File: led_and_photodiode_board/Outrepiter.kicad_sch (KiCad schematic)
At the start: 10 parts, among them U10 LM2901

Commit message: ledphoto исправлена микросхема
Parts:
- removed U10: LM2901, symbol Comparator:LM2901
- added U1: LM2901, symbol Comparator:LM2901
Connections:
- net +24V: now also U1.3 (V+)
- net GNDA: now also U1.12 (V-)
- net OUT1: now also U1.2
- net OUT2: now also U1.1
- net OUT3: now also U1.13
- net OUT4: now also U1.14
- net at R19.2: now also U1.10 (-)
- net at R23.2: now also U1.11 (+)
- net at R21.2: now also U1.5 (+)
- net at R26.2: now also U1.4 (-)
- net at R24.2: now also U1.9 (+)
- net at R20.2: now also U1.8 (-)
- net at R22.2: now also U1.7 (+)
- net at R18.2: now also U1.6 (-)

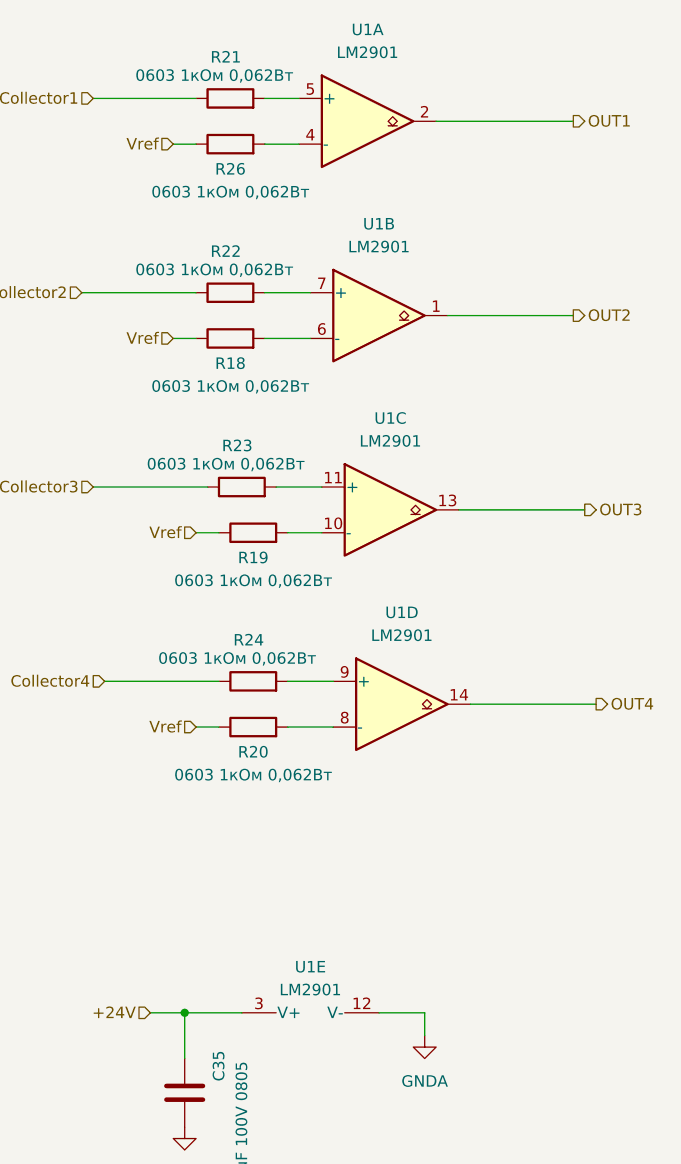
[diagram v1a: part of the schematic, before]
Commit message: ledphoto коррекция схемы
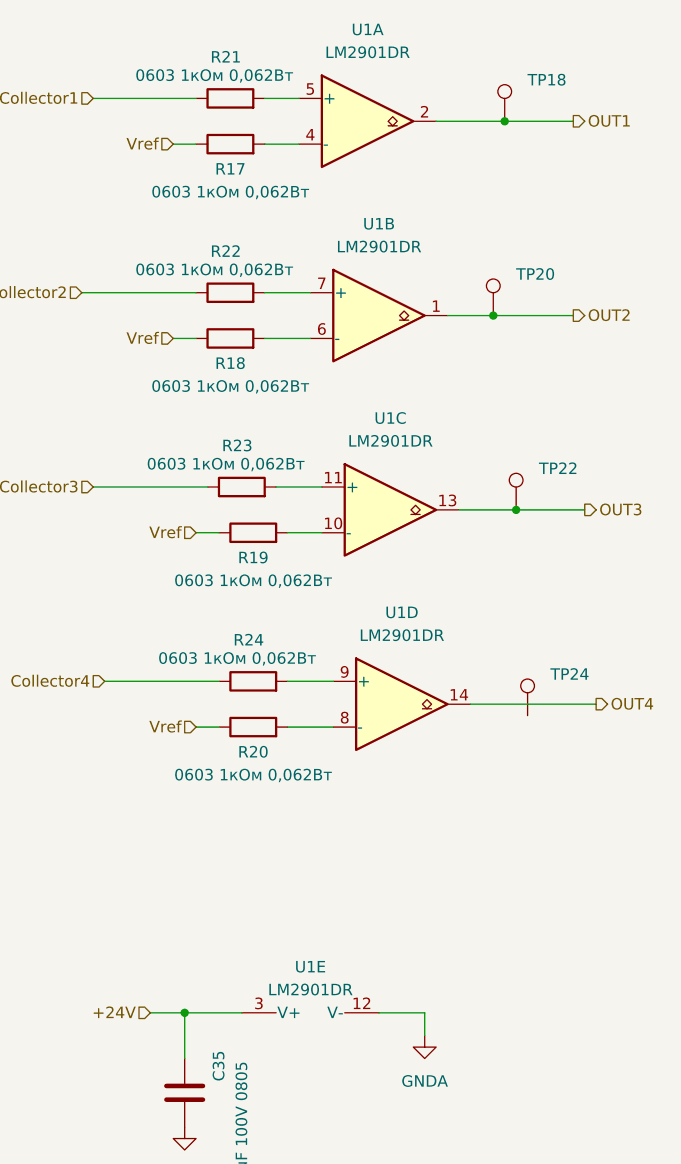
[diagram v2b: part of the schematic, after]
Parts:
- added TP18, TP20, TP22, TP24: TestPoint, TestPoint:TestPoint_Pad_D1.0mm, symbol Connector:TestPoint
- C35: footprint PCM_Resistor_SMD_AKL:R_0805_2012Metric_Pad1.20x1.40mm_HandSolder -> Capacitor_SMD:C_0805_2012Metric
- R17: renamed from R26; footprint (none) -> Resistor_SMD:R_0603_1608Metric
- R18, R19, R20, R21, R22, R23, R24: footprint (none) -> Resistor_SMD:R_0603_1608Metric
- U1: value LM2901 -> LM2901DR; footprint (none) -> Package_SO:SOIC-14_3.9x8.7mm_P1.27mm
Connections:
- net OUT1: now also TP18.1
- net OUT2: now also TP20.1
- net OUT3: now also TP22.1

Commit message: ledphoto обновлена схема и pcb
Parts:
- C35: value 0,1uF 100V 0805 -> 0805 0,1uF 100V
- R17, R18, R19, R20, R21, R22, R23, R24: value 0603 1кОм 0,062Вт -> 0603 1 кОм±5%-0,062Вт
- U1: value LM2901DR -> LM2901DR (SOIC-14)
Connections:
- net OUT4: now also TP24.1
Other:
- moved on the sheet: TP24
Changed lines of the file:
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@@
 		(color 0 0 0 0)
 	)
+	(junction
+		(at 160.02 118.11)
+		(diameter 0)
+		(color 0 0 0 0)
+	)
 	(wire
 		(pts
@@
 	(wire
 		(pts
+			(xy 160.02 118.11) (xy 153.67 118.11)
+		)
+		(stroke
+			(width 0)
+			(type default)
+		)
+	)
+	(wire
+		(pts
 			(xy 152.4 96.52) (xy 158.75 96.52)
 		)
@@
 	(wire
 		(pts
+			(xy 161.29 53.34) (xy 157.48 53.34)
+		)
+		(stroke
+			(width 0)
+			(type default)
+		)
+	)
+	(wire
+		(pts
+			(xy 162.56 74.93) (xy 156.21 74.93)
+		)
+		(stroke
+			(width 0)
+			(type default)
+		)
+	)
+	(wire
+		(pts
 			(xy 121.92 152.4) (xy 121.92 157.48)
 		)
@@
 	(wire
 		(pts
-			(xy 156.21 74.93) (xy 165.1 74.93)
+			(xy 161.29 96.52) (xy 158.75 96.52)
+		)
+		(stroke
+			(width 0)
+			(type default)
+		)
+	)
+	(wire
+		(pts
+			(xy 162.56 73.66) (xy 165.1 73.66)
 		)
 		(stroke
@@
 	(wire
 		(pts
-			(xy 153.67 118.11) (xy 167.64 118.11)
-		)
-		(stroke
-			(width 0)
-			(type default)
-		)
-	)
-	(wire
-		(pts
 			(xy 121.92 152.4) (xy 128.27 152.4)
 		)
@@
 	(wire
 		(pts
+			(xy 161.29 95.25) (xy 161.29 96.52)
+		)
+		(stroke
+			(width 0)
+			(type default)
+		)
+	)
+	(wire
+		(pts
 			(xy 120.65 55.88) (xy 123.19 55.88)
 		)
@@
 	(wire
 		(pts
-			(xy 157.48 53.34) (xy 165.1 53.34)
+			(xy 161.29 52.07) (xy 165.1 52.07)
 		)
 		(stroke
@@
 	(wire
 		(pts
+			(xy 160.02 118.11) (xy 167.64 118.11)
+		)
+		(stroke
+			(width 0)
+			(type default)
+		)
+	)
+	(wire
+		(pts
 			(xy 130.81 55.88) (xy 134.62 55.88)
 		)
@@
 	(wire
 		(pts
-			(xy 158.75 96.52) (xy 166.37 96.52)
+			(xy 161.29 95.25) (xy 166.37 95.25)
+		)
+		(stroke
+			(width 0)
+			(type default)
+		)
+	)
+	(wire
+		(pts
+			(xy 162.56 73.66) (xy 162.56 74.93)
+		)
+		(stroke
+			(width 0)
+			(type default)
+		)
+	)
+	(wire
+		(pts
+			(xy 161.29 52.07) (xy 161.29 53.34)
 		)
 		(stroke
@@
 	(hierarchical_label "OUT2"
 		(shape output)
-		(at 165.1 74.93 0)
+		(at 165.1 73.66 0)
 		(fields_autoplaced yes)
 		(effects
@@
 	(hierarchical_label "OUT1"
 		(shape output)
-		(at 165.1 53.34 0)
+		(at 165.1 52.07 0)
 		(fields_autoplaced yes)
 		(effects
@@
 	(hierarchical_label "OUT3"
 		(shape output)
-		(at 166.37 96.52 0)
+		(at 166.37 95.25 0)
 		(fields_autoplaced yes)
 		(effects
@@
 			)
 		)
-		(property "Value" "LM2901DR"
+		(property "Value" "LM2901DR (SOIC-14)"
 			(at 144.78 88.9 0)
 			(effects
@@
 			)
 		)
-		(property "Value" "0603 1кОм 0,062Вт"
+		(property "Value" "0603 1 кОм±5%-0,062Вт"
 			(at 125.222 48.26 90)
 			(effects
@@
 			)
 		)
-		(property "Value" "0603 1кОм 0,062Вт"
+		(property "Value" "0603 1 кОм±5%-0,062Вт"
 			(at 127.762 113.03 90)
 			(effects
@@
 			)
 		)
-		(property "Value" "LM2901DR"
+		(property "Value" "LM2901DR (SOIC-14)"
 			(at 146.05 110.49 0)
 			(effects
@@
 			)
 		)
-		(property "Value" "0603 1кОм 0,062Вт"
+		(property "Value" "0603 1 кОм±5%-0,062Вт"
 			(at 127 61.214 90)
 			(effects
@@
 			)
 		)
-		(property "Value" "LM2901DR"
+		(property "Value" "LM2901DR (SOIC-14)"
 			(at 142.24 45.72 0)
 			(effects
@@
 			)
 		)
-		(property "Value" "0603 1кОм 0,062Вт"
+		(property "Value" "0603 1 кОм±5%-0,062Вт"
 			(at 129.54 125.984 90)
 			(effects
@@
 			)
 		)
-		(property "Value" "0603 1кОм 0,062Вт"
+		(property "Value" "0603 1 кОм±5%-0,062Вт"
 			(at 129.54 104.394 90)
 			(effects
@@
 			)
 		)
-		(property "Value" "0,1uF 100V 0805"
+		(property "Value" "0805 0,1uF 100V"
 			(at 128.27 172.72 90)
 			(effects
@@
 			)
 		)
-		(property "Value" "0603 1кОм 0,062Вт"
+		(property "Value" "0603 1 кОм±5%-0,062Вт"
 			(at 125.222 69.85 90)
 			(effects
@@
 			)
 		)
-		(property "Value" "0603 1кОм 0,062Вт"
+		(property "Value" "0603 1 кОм±5%-0,062Вт"
 			(at 126.492 91.44 90)
 			(effects
@@
 			)
 		)
-		(property "Value" "0603 1кОм 0,062Вт"
+		(property "Value" "0603 1 кОм±5%-0,062Вт"
 			(at 127 82.804 90)
 			(effects
@@
 			)
 		)
-		(property "Value" "LM2901DR"
+		(property "Value" "LM2901DR (SOIC-14)"
 			(at 143.51 67.31 0)
 			(effects
@@
 	(symbol
 		(lib_id "Connector:TestPoint")
-		(at 160.02 119.38 0)
+		(at 160.02 118.11 0)
 		(unit 1)
 		(exclude_from_sim no)
@@
 		(fields_autoplaced yes)
 		(property "Reference" "TP24"
-			(at 162.56 114.8079 0)
+			(at 162.56 113.5379 0)
 			(effects
 				(font
@@
 		)
 		(property "Value" "TestPoint"
-			(at 162.56 117.3479 0)
+			(at 162.56 116.0779 0)
 			(effects
 				(font
@@
 		)
 		(property "Footprint" "TestPoint:TestPoint_Pad_D1.0mm"
-			(at 165.1 119.38 0)
+			(at 165.1 118.11 0)
 			(effects
 				(font
@@
 		)
 		(property "Datasheet" "~"
-			(at 165.1 119.38 0)
+			(at 165.1 118.11 0)
 			(effects
 				(font
@@
 		)
 		(property "Description" "test point"
-			(at 160.02 119.38 0)
+			(at 160.02 118.11 0)
 			(effects
 				(font
@@
 			)
 		)
-		(property "Value" "LM2901DR"
+		(property "Value" "LM2901DR (SOIC-14)"
 			(at 135.89 149.86 90)
 			(effects

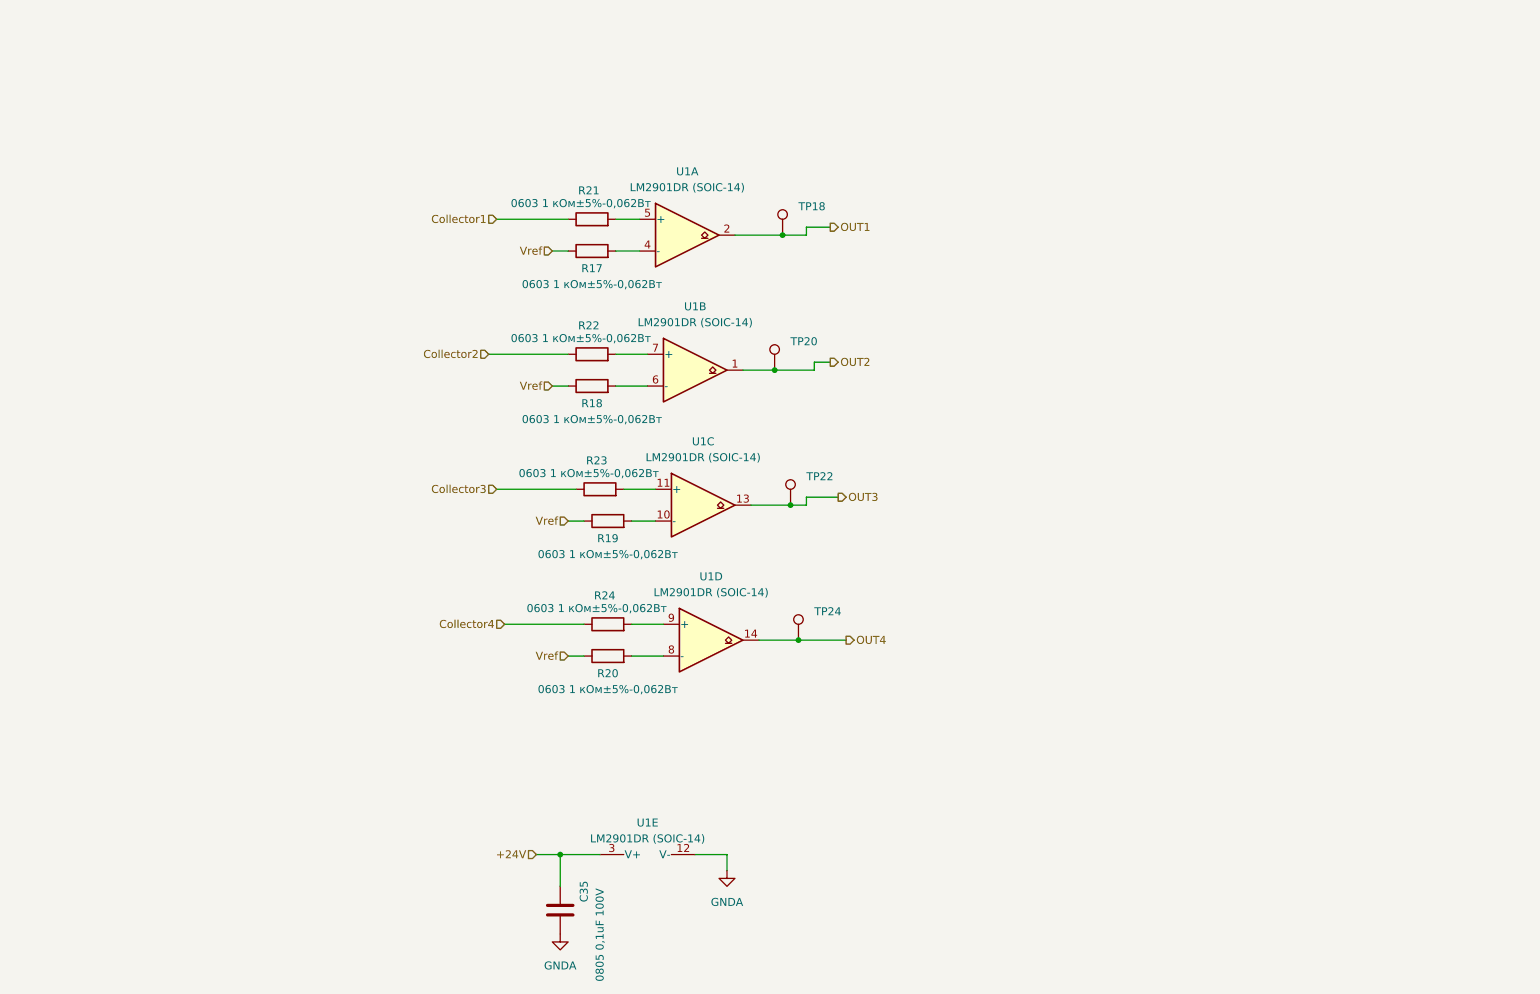
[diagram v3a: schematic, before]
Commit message: ledphoto замена компаратора на операционник, добавлен снаббер
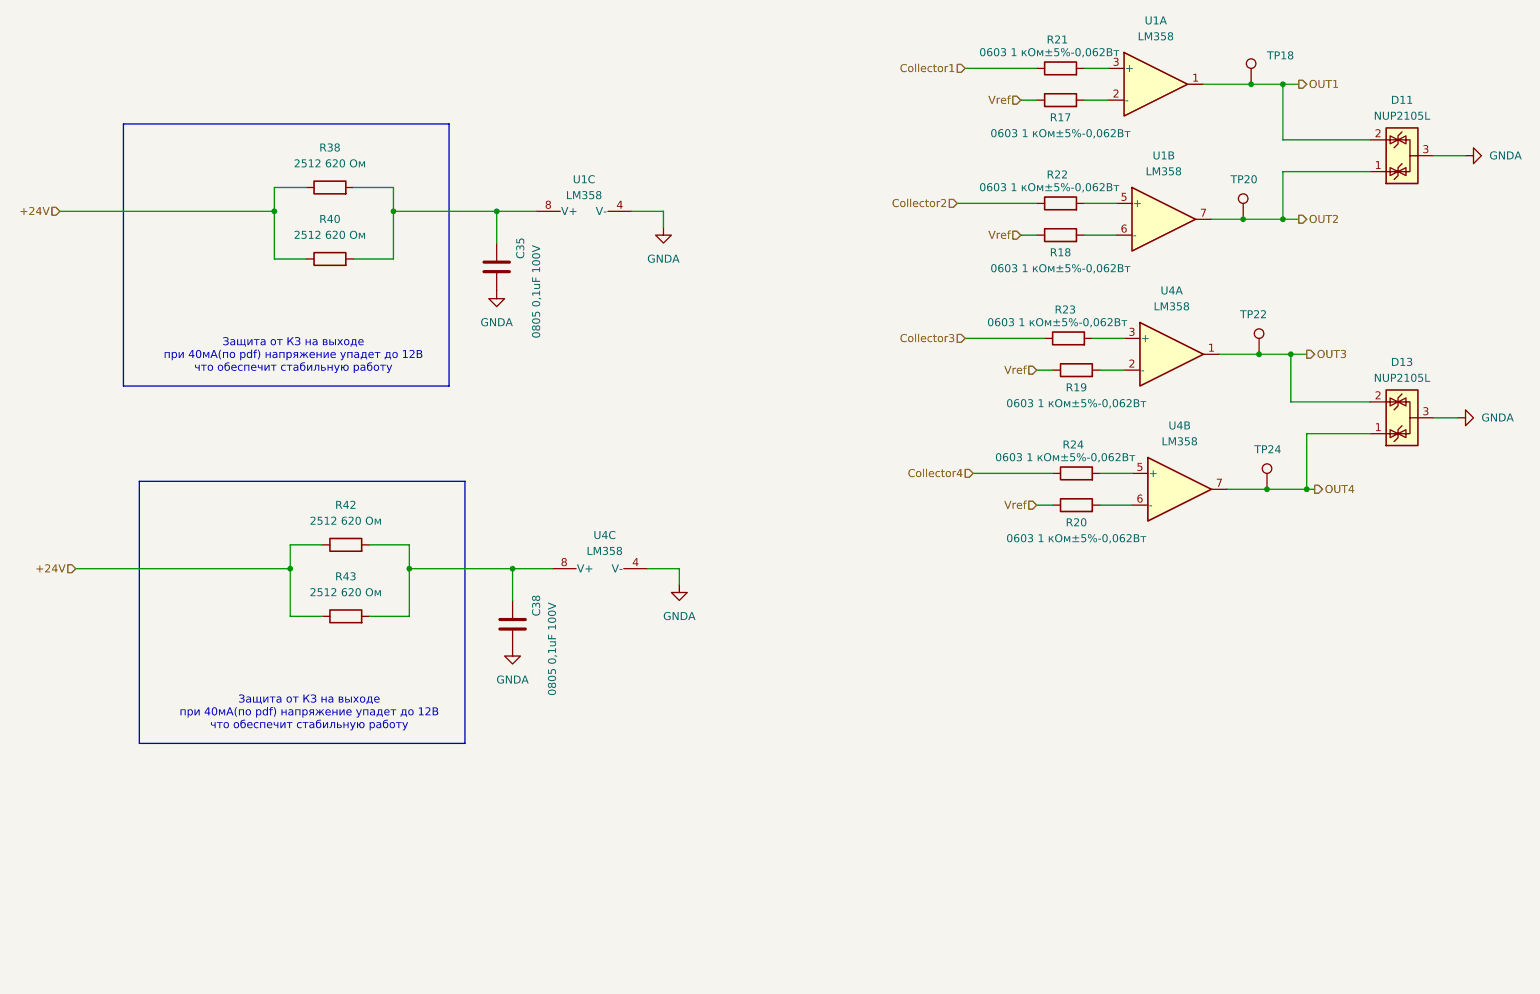
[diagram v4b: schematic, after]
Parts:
- removed U1: LM2901DR (SOIC-14), Package_SO:SOIC-14_3.9x8.7mm_P1.27mm, symbol Comparator:LM2901
- added C38: 0805 0,1uF 100V, Capacitor_SMD:C_0805_2012Metric, symbol Device:C
- added D11, D13: NUP2105L, Package_TO_SOT_SMD:SOT-23, symbol Power_Protection:NUP2105L
- added R38, R40, R42, R43: 2512 620 Ом, Resistor_SMD:R_2512_6332Metric, symbol Device:R
- added U1, U4: LM358, symbol Amplifier_Operational:LM358
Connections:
- net +24V: now also R38.1, R40.1, R42.1, R43.1; no longer C35.1
- net GNDA: now also C38.2, D11.3 (A), D13.3 (A), U1.4 (V-), U4.4 (V-)
- net OUT1: now also D11.2 (K), U1.1
- net OUT2: now also D11.1 (K), U1.7
- net OUT3: now also D13.2 (K), U4.1
- net OUT4: now also D13.1 (K), U4.7
- net at R19.2: now also U4.2 (-)
- net at R23.2: now also U4.3 (+)
- net at R21.2: now also U1.3 (+)
- net at R24.2: now also U4.5 (+)
- net at R20.2: now also U4.6 (-)
- net at R17.2: now also U1.2 (-)
- net at R22.2: now also U1.5 (+)
- net at R18.2: now also U1.6 (-)
- new net: C38.1, R42.2, R43.2, U4.8 (V+)
- new net: C35.1, R38.2, R40.2, U1.8 (V+)
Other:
- note added: "Защита от КЗ на выходе при 40мА(по pdf) напряжение упадет до 12В что обеспечит стабильную работу"
- moved on the sheet: C35, R17, R18, R19, R20, R21, R22, R23, R24, TP18, TP20, TP22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

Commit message: led and photo топология
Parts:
- U1, U4: footprint (none) -> Package_SO:SOIC-8_3.9x4.9mm_P1.27mm
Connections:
- net OUT3: now also D13.1 (K); no longer D13.2 (K)
- net OUT4: now also D13.2 (K); no longer D13.1 (K)
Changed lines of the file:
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@@
 			)
 		)
-		(property "Footprint" ""
+		(property "Footprint" "Package_SO:SOIC-8_3.9x4.9mm_P1.27mm"
 			(at 220.98 93.98 0)
 			(effects
@@
 			)
 		)
-		(property "Footprint" ""
+		(property "Footprint" "Package_SO:SOIC-8_3.9x4.9mm_P1.27mm"
 			(at 217.17 29.21 0)
 			(effects
@@
 			)
 		)
-		(property "Footprint" ""
+		(property "Footprint" "Package_SO:SOIC-8_3.9x4.9mm_P1.27mm"
 			(at 218.44 50.8 0)
 			(effects
@@
 			)
 		)
-		(property "Footprint" ""
+		(property "Footprint" "Package_SO:SOIC-8_3.9x4.9mm_P1.27mm"
 			(at 128.27 104.14 0)
 			(effects
@@
 			)
 		)
-		(property "Footprint" ""
+		(property "Footprint" "Package_SO:SOIC-8_3.9x4.9mm_P1.27mm"
 			(at 125.73 46.99 0)
 			(effects
@@
 		(lib_id "Power_Protection:NUP2105L")
 		(at 256.54 82.55 90)
-		(unit 1)
-		(exclude_from_sim no)
-		(in_bom yes)
-		(on_board yes)
-		(dnp no)
-		(fields_autoplaced yes)
+		(mirror x)
+		(unit 1)
+		(exclude_from_sim no)
+		(in_bom yes)
+		(on_board yes)
+		(dnp no)
 		(property "Reference" "D13"
-			(at 256.54 73.66 90)
+			(at 256.54 91.44 90)
 			(effects
 				(font
@@
 		)
 		(property "Value" "NUP2105L"
-			(at 256.54 76.2 90)
+			(at 256.54 88.9 90)
 			(effects
 				(font
@@
 		)
 		(property "Footprint" "Package_TO_SOT_SMD:SOT-23"
-			(at 257.81 76.835 0)
+			(at 257.81 88.265 0)
 			(effects
 				(font
@@
 		)
 		(property "Datasheet" "https://www.onsemi.com/pub_link/Collateral/NUP2105L-D.PDF"
-			(at 253.365 79.375 0)
+			(at 253.365 85.725 0)
 			(effects
 				(font
@@
 			)
 		)
-		(property "Footprint" ""
+		(property "Footprint" "Package_SO:SOIC-8_3.9x4.9mm_P1.27mm"
 			(at 219.71 72.39 0)
 			(effects

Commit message: update schemas
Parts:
- TP18, TP20, TP22, TP24: now left out of the parts list
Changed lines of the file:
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@@
 		(unit 1)
 		(exclude_from_sim no)
-		(in_bom yes)
+		(in_bom no)
 		(on_board yes)
 		(dnp no)
@@
 		(unit 1)
 		(exclude_from_sim no)
-		(in_bom yes)
+		(in_bom no)
 		(on_board yes)
 		(dnp no)
@@
 		(unit 1)
 		(exclude_from_sim no)
-		(in_bom yes)
+		(in_bom no)
 		(on_board yes)
 		(dnp no)
@@
 		(unit 1)
 		(exclude_from_sim no)
-		(in_bom yes)
-		(on_board yes)
-		(dnp no)
+		(in_bom no)
+		(on_board yes)
+		(dnp no)
